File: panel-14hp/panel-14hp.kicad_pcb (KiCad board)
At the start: 2 copper layers, 70.8 x 128.5 mm, 4 parts

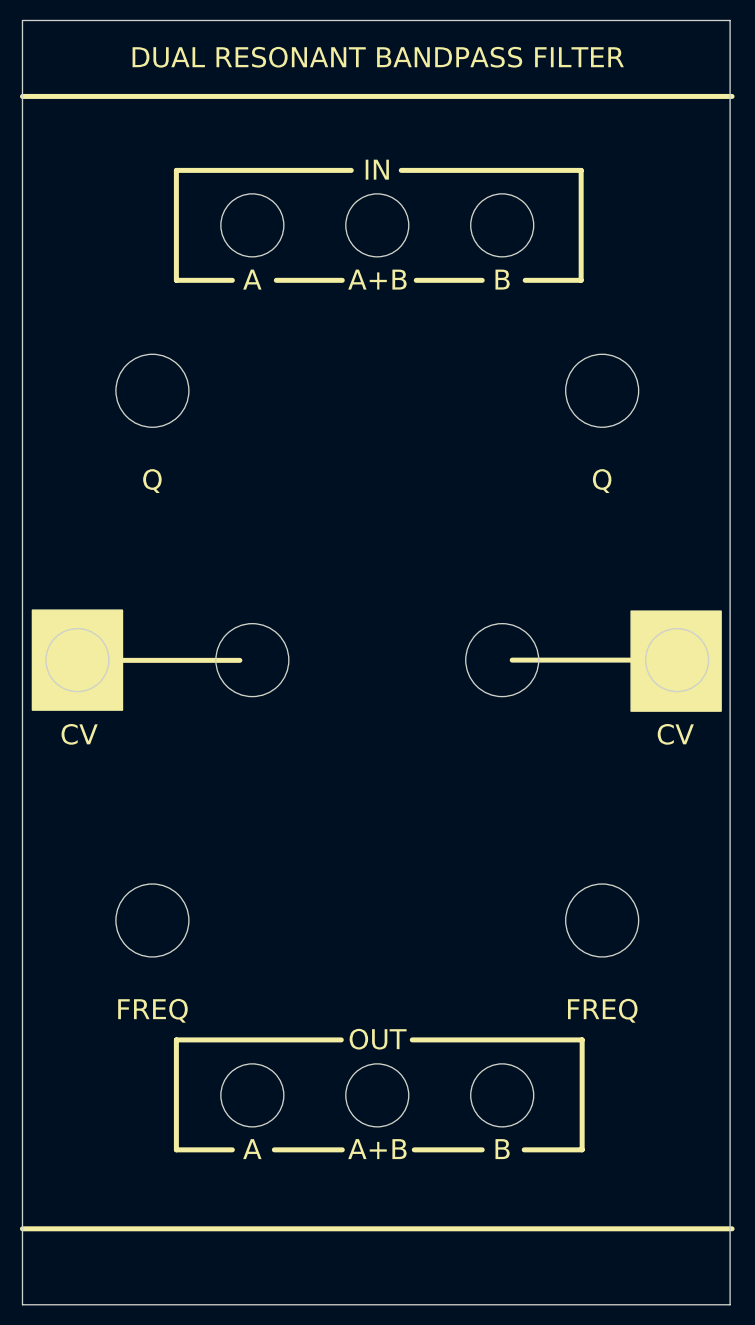
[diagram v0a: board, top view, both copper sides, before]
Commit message: Changed inputs to circles on panels
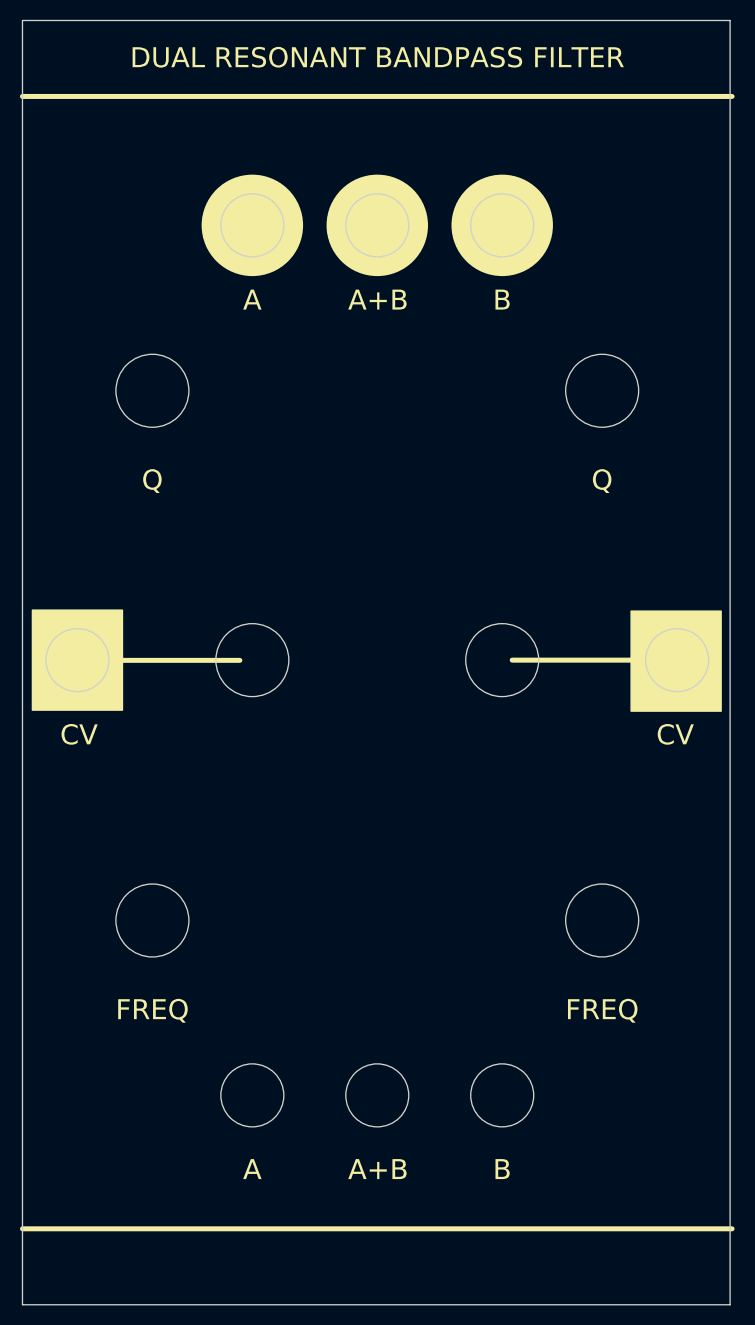
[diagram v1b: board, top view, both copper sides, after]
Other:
- board text removed: "IN"
- board text removed: "OUT"
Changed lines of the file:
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@@
   )
   (gr_line (start 0 7.6) (end 71 7.6) (layer "F.SilkS") (width 0.5))
-  (gr_line (start 50.3 26) (end 55.9 26) (layer "F.SilkS") (width 0.5))
   (gr_line (start 0 120.9) (end 71 120.9) (layer "F.SilkS") (width 0.5))
-  (gr_line (start 15.4 113) (end 21 113) (layer "F.SilkS") (width 0.5))
-  (gr_line (start 55.9 15) (end 37.9 15) (layer "F.SilkS") (width 0.5))
-  (gr_line (start 25.4 26) (end 32 26) (layer "F.SilkS") (width 0.5))
-  (gr_line (start 25.2 113) (end 32 113) (layer "F.SilkS") (width 0.5))
-  (gr_line (start 56 113) (end 56 102) (layer "F.SilkS") (width 0.5))
-  (gr_line (start 31.9 102) (end 15.4 102) (layer "F.SilkS") (width 0.5))
+  (gr_circle (center 23 20.5) (end 28 20.5) (layer "F.SilkS") (width 0.15) (fill solid))
+  (gr_circle (center 35.5 20.5) (end 40.5 20.5) (layer "F.SilkS") (width 0.15) (fill solid))
   (gr_rect (start 1 59) (end 10 69) (layer "F.SilkS") (width 0.15) (fill solid))
-  (gr_line (start 55.9 26) (end 55.9 15) (layer "F.SilkS") (width 0.5))
-  (gr_line (start 39.2 113) (end 46 113) (layer "F.SilkS") (width 0.5))
-  (gr_line (start 56 102) (end 39 102) (layer "F.SilkS") (width 0.5))
-  (gr_line (start 50.2 113) (end 56 113) (layer "F.SilkS") (width 0.5))
+  (gr_circle (center 48 20.5) (end 53 20.5) (layer "F.SilkS") (width 0.15) (fill solid))
   (gr_line (start 5.75 64.025) (end 21.75 64.025) (layer "F.SilkS") (width 0.5))
-  (gr_line (start 15.4 102) (end 15.4 113) (layer "F.SilkS") (width 0.5))
-  (gr_line (start 15.4 26) (end 21 26) (layer "F.SilkS") (width 0.5))
-  (gr_line (start 32.9 15) (end 15.4 15) (layer "F.SilkS") (width 0.5))
-  (gr_line (start 15.4 15) (end 15.4 26) (layer "F.SilkS") (width 0.5))
-  (gr_line (start 39.4 26) (end 46 26) (layer "F.SilkS") (width 0.5))
   (gr_line (start 49 64) (end 65 64) (layer "F.SilkS") (width 0.5))
   (gr_rect (start 60.9 59.1) (end 69.9 69.1) (layer "F.SilkS") (width 0.15) (fill solid))
@@
     (effects (font (size 2 2) (thickness 0.3)))
   )
-  (gr_text "A" (at 23 26) (layer "F.SilkS")
+  (gr_text "A" (at 23 28) (layer "F.SilkS")
     (effects (font (size 2 2) (thickness 0.3)))
   )
@@
     (effects (font (size 2 2) (thickness 0.3)))
   )
-  (gr_text "A+B" (at 35.6 26) (layer "F.SilkS")
+  (gr_text "A+B" (at 35.6 28) (layer "F.SilkS")
     (effects (font (size 2 2) (thickness 0.3)))
   )
@@
     (effects (font (size 2 2) (thickness 0.3)))
   )
-  (gr_text "B" (at 48 26) (layer "F.SilkS")
+  (gr_text "B" (at 48 28) (layer "F.SilkS")
     (effects (font (size 2 2) (thickness 0.3)))
   )
@@
     (effects (font (size 2 2) (thickness 0.4)))
   )
-  (gr_text "A" (at 23 113) (layer "F.SilkS")
+  (gr_text "A" (at 23 115) (layer "F.SilkS")
     (effects (font (size 2 2) (thickness 0.3)))
   )
-  (gr_text "OUT" (at 35.5 102) (layer "F.SilkS")
+  (gr_text "B" (at 48 115) (layer "F.SilkS")
     (effects (font (size 2 2) (thickness 0.3)))
   )
-  (gr_text "B" (at 48 113) (layer "F.SilkS")
+  (gr_text "A+B" (at 35.6 115) (layer "F.SilkS")
     (effects (font (size 2 2) (thickness 0.3)))
   )
-  (gr_text "IN" (at 35.5 15) (layer "F.SilkS")
-    (effects (font (size 2 2) (thickness 0.3)))
-  )
-  (gr_text "A+B" (at 35.6 113) (layer "F.SilkS")
-    (effects (font (size 2 2) (thickness 0.3)))
-  )
